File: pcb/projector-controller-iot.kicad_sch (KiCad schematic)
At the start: 0 parts

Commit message: version where the esp sticks out
Signed-off-by: 3nt3 <gott@3nt3.de>
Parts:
- added C1, C10, C2, C4, C5, C6, C7: 100n, Capacitor_SMD:C_0603_1608Metric_Pad1.08x0.95mm_HandSolder, symbol Device:C
- added C3: 22u, Capacitor_SMD:C_0603_1608Metric_Pad1.08x0.95mm_HandSolder, symbol Device:C
- added C8, C9: 1u, Capacitor_SMD:C_0603_1608Metric_Pad1.08x0.95mm_HandSolder, symbol Device:C
- added D1, D2: LED, LED_SMD:LED_0603_1608Metric_Pad1.05x0.95mm_HandSolder, symbol Device:LED
- added D3: LED, symbol Device:LED
- added H1, H2, H3, H4: MountingHole_Pad, MountingHole:MountingHole_4.5mm_Pad_Via, symbol Mechanical:MountingHole_Pad
- added J1: DE9_Pins, Connector_Dsub:DSUB-9_Pins_Horizontal_P2.77x2.84mm_EdgePinOffset9.40mm, symbol Connector:DE9_Pins
- added J2: USB_C_Receptacle, Connector_USB:USB_C_Receptacle_HRO_TYPE-C-31-M-12, symbol Connector:USB_C_Receptacle
- added J3, J4: Conn_01x04_Socket, Connector_JST:JST_XH_B4B-XH-AM_1x04_P2.50mm_Vertical, symbol Connector:Conn_01x04_Socket
- added J5: Barrel_Jack, easyeda2kicad:DC-IN-TH_DC005, symbol Connector:Barrel_Jack
- added JP1: Jumper_2_Open, Connector_PinHeader_2.54mm:PinHeader_1x02_P2.54mm_Vertical, symbol Jumper:Jumper_2_Open
- added R1: 5K1, Resistor_SMD:R_0603_1608Metric_Pad0.98x0.95mm_HandSolder, symbol Device:R
- added R2: 5k1, Resistor_SMD:R_0603_1608Metric_Pad0.98x0.95mm_HandSolder, symbol Device:R
- added R3, R4, R5: 1K, Resistor_SMD:R_0603_1608Metric_Pad0.98x0.95mm_HandSolder, symbol Device:R
- added R6: 1K, symbol Device:R
- added SW1: SW_Push, easyeda2kicad:SW-SMD_4P-L5.1-W5.1-P3.70-LS6.5-TL_H1.5, symbol Switch:SW_Push
- added U1: ESP32-S3-WROOM-1, RF_Module:ESP32-S3-WROOM-1, symbol Espressif:ESP32-S3-WROOM-1
- added U2: SP3232EEN-L/TR, Package_SO:JEITA_SOIC-16_3.9x9.9mm_P1.27mm, symbol 3nt3:SP3232E
- added U3: LP5907MFX-3.3, Package_TO_SOT_SMD:SOT-23-5, symbol Regulator_Linear:LP5907MFX-3.3
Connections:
- new net: C2.2, R3.2, SW1.2, U1.3 (EN)
- new net: C7.2, U2.6 (V-)
- new net: C4.1, U2.2 (V+)
- new net: JP1.1 (A), U1.27 (GPIO0/BOOT)
- new net: D1.1 (K), R4.1
- new net: C6.1, U2.4 (C2+)
- new net: C6.2, U2.5 (C2-)
- new net: D3.1 (K), R6.1
- new net: C5.1, U2.1 (C1+)
- new net: C5.2, U2.3 (C1-)
- new net: D2.1 (K), R5.1
- new net: D2.2 (A), U1.12 (GPIO8/TOUCH8/ADC1_CH7/SUBSPICS1)
- new net: D1.2 (A), U1.6 (GPIO6/TOUCH6/ADC1_CH5)
- new net: J2.A5 (CC1), R2.1
- new net: J2.B5 (CC2), R1.1
- new net +3V3: C1.1, C10.1, C3.1, C9.1, D3.2 (A), J3.1 (Pin_1), R3.1, U1.2 (3V3), U2.16 (VCC), U3.5 (OUT)
- new net GND: C1.2, C10.2, C2.1, C3.2, C4.2, C7.1, C8.2, C9.2, H1.1, H2.1, H3.1, H4.1, J1.5, J2.A1 (GND), J2.A12 (GND), J2.B1 (GND), J2.B12 (GND), J3.4 (Pin_4), J5.2, JP1.2 (B), R1.2, R2.2, R4.2, R5.2, R6.2, SW1.1, U1.1 (GND), U1.40 (GND), U1.41 (GND), U2.15 (GND), U3.2 (GND)
- new net RX: J1.2, U2.13 (R1IN)
- new net TCK: J4.4 (Pin_4), U1.32 (MTCK/GPIO39/CLK_OUT3/SUBSPICS1)
- new net TDI: J4.2 (Pin_2), U1.34 (MTDI/GPIO41/CLK_OUT1)
- new net TDO: J4.3 (Pin_3), U1.33 (MTDO/GPIO40/CLK_OUT2)
- new net TMS: J4.1 (Pin_1), U1.35 (MTMS/GPIO42)
- new net TX: J1.3, U2.14 (T1OUT)
- new net U0RX: J3.3 (Pin_3), U1.36 (U0RXD/GPIO44/CLK_OUT2)
- new net U0TX: J3.2 (Pin_2), U1.37 (U0TXD/GPIO43/CLK_OUT1)
- new net U1RX: U1.11 (GPIO18/U1RXD/ADC2_CH7/CLK_OUT3), U2.12 (R1OUT)
- new net U1TX: U1.10 (GPIO17/U1TXD/ADC2_CH6), U2.11 (T1IN)
- new net USB_D+: J2.A6 (D+), J2.B6 (D+), U1.13 (GPIO19/U1RTS/ADC2_CH8/CLK_OUT2/USB_D-)
- new net USB_D-: J2.A7 (D-), J2.B7 (D-), U1.14 (GPIO20/U1CTS/ADC2_CH9/CLK_OUT1/USB_D+)
- new net VBUS: C8.1, J2.A4 (VBUS), J2.A9 (VBUS), J2.B4 (VBUS), J2.B9 (VBUS), J5.1, U3.1 (IN), U3.3 (EN)
- no-connect marks 0 -> 24

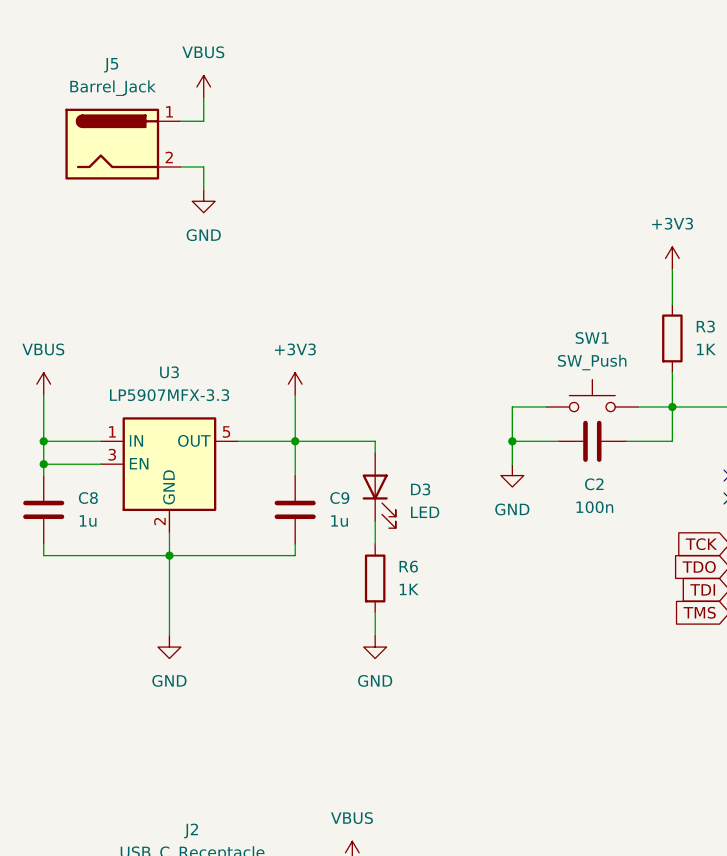
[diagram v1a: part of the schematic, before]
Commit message: make the esp not stick out
Signed-off-by: 3nt3 <gott@3nt3.de>
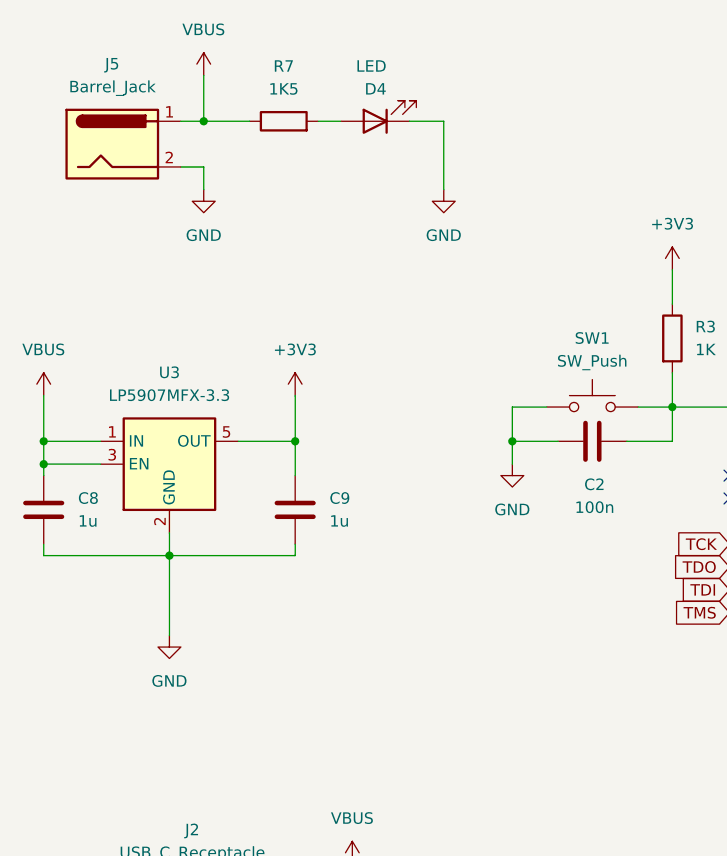
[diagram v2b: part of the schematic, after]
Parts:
- removed D3: LED, symbol Device:LED
- removed R6: 1K, symbol Device:R
- added D4: LED, kicad-lib:LED_0603_1608Metric_Pad1.05x0.95mm_HandSolder_Triangle, symbol Device:LED
- added R7: 1K5, Resistor_SMD:R_0603_1608Metric_Pad0.98x0.95mm_HandSolder, symbol Device:R
- D1, D2: footprint LED_SMD:LED_0603_1608Metric_Pad1.05x0.95mm_HandSolder -> kicad-lib:LED_0603_1608Metric_Pad1.05x0.95mm_HandSolder_Triangle
- J1: footprint Connector_Dsub:DSUB-9_Pins_Horizontal_P2.77x2.84mm_EdgePinOffset9.40mm -> easyeda2kicad:DB9-TH_LD09P33E4GV00LF
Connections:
- net GND: now also D4.1 (K)
- net VBUS: now also R7.1
- new net: D4.2 (A), R7.2

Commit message: make fanout make sense
Signed-off-by: 3nt3 <gott@3nt3.de>
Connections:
- net at D2.2 (A): now also U1.38 (GPIO2/TOUCH2/ADC1_CH1); no longer U1.12 (GPIO8/TOUCH8/ADC1_CH7/SUBSPICS1)
- net at U1.39 (GPIO1/TOUCH1/ADC1_CH0): now also D1.2 (A)
- net at U1.6 (GPIO6/TOUCH6/ADC1_CH5): no longer D1.2 (A)
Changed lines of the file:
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@@
+	(wire
+		(pts
+			(xy 184.15 76.2) (xy 195.58 76.2)
+		)
+		(stroke
+			(width 0)
+			(type default)
+		)
+	)
+	(wire
+		(pts
+			(xy 184.15 78.74) (xy 191.77 78.74)
+		)
+		(stroke
+			(width 0)
+			(type default)
+		)
+	)
 	(wire
 		(pts
@@
 	(wire
 		(pts
-			(xy 184.15 88.9) (xy 201.93 88.9)
-		)
-		(stroke
-			(width 0)
-			(type default)
-		)
-	)
-	(wire
-		(pts
 			(xy 236.22 39.37) (xy 233.68 39.37)
 		)
@@
 	(wire
 		(pts
-			(xy 184.15 93.98) (xy 201.93 93.98)
-		)
-		(stroke
-			(width 0)
-			(type default)
-		)
-	)
-	(wire
-		(pts
 			(xy 228.6 124.46) (xy 231.14 124.46)
 		)
@@
 	(wire
 		(pts
+			(xy 191.77 93.98) (xy 201.93 93.98)
+		)
+		(stroke
+			(width 0)
+			(type default)
+		)
+	)
+	(wire
+		(pts
 			(xy 226.06 88.9) (xy 220.98 88.9)
 		)
@@
 	(wire
 		(pts
+			(xy 191.77 93.98) (xy 191.77 78.74)
+		)
+		(stroke
+			(width 0)
+			(type default)
+		)
+	)
+	(wire
+		(pts
 			(xy 138.43 36.83) (xy 148.59 36.83)
 		)
@@
 	(wire
 		(pts
+			(xy 195.58 88.9) (xy 201.93 88.9)
+		)
+		(stroke
+			(width 0)
+			(type default)
+		)
+	)
+	(wire
+		(pts
 			(xy 257.81 132.08) (xy 262.89 132.08)
 		)
@@
 		)
 		(stroke
+			(width 0)
+			(type default)
+		)
+	)
+	(wire
+		(pts
+			(xy 195.58 76.2) (xy 195.58 88.9)
+		)
+		(stroke

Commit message: Bro idk
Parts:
- added JP2, JP3: Jumper_3_Open, symbol Jumper:Jumper_3_Open
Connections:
- net RX: now also JP2.2 (C), JP3.2 (C); no longer U2.13 (R1IN)
- net TX: now also JP2.3 (B), JP3.3 (B); no longer U2.14 (T1OUT)
- net USB_D+: now also U1.14 (GPIO20/U1CTS/ADC2_CH9/CLK_OUT1/USB_D+); no longer U1.13 (GPIO19/U1RTS/ADC2_CH8/CLK_OUT2/USB_D-)
- net USB_D-: now also U1.13 (GPIO19/U1RTS/ADC2_CH8/CLK_OUT2/USB_D-); no longer U1.14 (GPIO20/U1CTS/ADC2_CH9/CLK_OUT1/USB_D+)
- new net: JP3.1 (A), U2.13 (R1IN)
- new net: JP2.1 (A), U2.14 (T1OUT)
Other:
- note added: "This abomination is there for things that swap RX and TX"
- moved on the sheet: C1, C10, C2, C3, C4, C5, C6, C7, C8, C9, D1, D2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
